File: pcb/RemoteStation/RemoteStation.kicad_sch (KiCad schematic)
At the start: 4 parts, among them J1 Conn_01x04, J2 Conn_01x02, J3 Conn_01x02, J4 Conn_01x04

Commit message: update
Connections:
- no-connect marks 0 -> 14
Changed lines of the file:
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@@
 	(generator_version "8.0")
 	(paper "A4")
+	(no_connect
+		(at 43.18 97.79)
+	)
+	(no_connect
+		(at 158.75 53.34)
+	)
+	(no_connect
+		(at 63.5 97.79)
+	)
+	(no_connect
+		(at 180.34 53.34)
+	)
+	(no_connect
+		(at 58.42 97.79)
+	)
+	(no_connect
+		(at 66.04 97.79)
+	)
+	(no_connect
+		(at 203.2 53.34)
+	)
+	(no_connect
+		(at 156.21 53.34)
+	)
+	(no_connect
+		(at 110.49 53.34)
+	)
+	(no_connect
+		(at 107.95 53.34)
+	)
+	(no_connect
+		(at 60.96 97.79)
+	)
+	(no_connect
+		(at 45.72 97.79)
+	)
+	(no_connect
+		(at 177.8 53.34)
+	)
+	(no_connect
+		(at 205.74 53.34)
+	)
 	(wire
 		(pts
@@
 		(pts
 			(xy 54.61 64.77) (xy 54.61 62.23)
+		)
+		(stroke
+			(width 0)
+			(type default)
+		)
+	)
+	(wire
+		(pts
+			(xy 29.21 173.99) (xy 29.21 176.53)
 		)
 		(stroke
@@
 	)
 	(symbol
+		(lib_id "power:PWR_FLAG")
+		(at 29.21 173.99 0)
+		(unit 1)
+		(exclude_from_sim no)
+		(in_bom yes)
+		(on_board yes)
+		(dnp no)
+		(fields_autoplaced yes)
+		(property "Reference" "#FLG01"
+			(at 29.21 172.085 0)
+			(effects
+				(font
+					(size 1.27 1.27)
+				)
+				(hide yes)
+			)
+		)
+		(property "Value" "PWR_FLAG"
+			(at 29.21 168.91 0)
+			(effects
+				(font
+					(size 1.27 1.27)
+				)
+			)
+		)
+		(property "Footprint" ""
+			(at 29.21 173.99 0)
+			(effects
+				(font
+					(size 1.27 1.27)
+				)
+				(hide yes)
+			)
+		)
+		(property "Datasheet" "~"
+			(at 29.21 173.99 0)
+			(effects
+				(font
+					(size 1.27 1.27)
+				)
+				(hide yes)
+			)
+		)
+		(property "Description" "Special symbol for telling ERC where power comes from"
+			(at 29.21 173.99 0)
+			(effects
+				(font
+					(size 1.27 1.27)
+				)
+				(hide yes)
+			)
+		)
+		(pin "1"
+		)
+		(instances
+			(project "RemoteStation"
+				(path "/5d20b266-567e-45c6-9e3e-145c2aea1daa"
+					(reference "#FLG01")
+					(unit 1)
+				)
+			)
+		)
+	)
+	(symbol
 		(lib_id "Connector_Generic:Conn_01x02")
 		(at 43.18 92.71 90)
@@
 					(unit 1)
 				)
+			)
+		)
+	)
+	(symbol
+		(lib_id "power:GND")
+		(at 29.21 176.53 0)
+		(unit 1)
+		(exclude_from_sim no)
+		(in_bom yes)
+		(on_board yes)
+		(dnp no)
+		(fields_autoplaced yes)
+		(property "Reference" "#PWR018"
+			(at 29.21 182.88 0)
+			(effects
+				(font
+					(size 1.27 1.27)
+				)
+				(hide yes)
+			)
+		)
+		(property "Value" "GND"
+			(at 29.21 181.61 0)
+			(effects
+				(font
+					(size 1.27 1.27)
+				)
+			)
+		)
+		(property "Footprint" ""
+			(at 29.21 176.53 0)
+			(effects
+				(font
+					(size 1.27 1.27)
+				)
+				(hide yes)
+			)
+		)
+		(property "Datasheet" ""
+			(at 29.21 176.53 0)
+			(effects
+				(font
+					(size 1.27 1.27)
+				)
+				(hide yes)
+			)
+		)
+		(property "Description" "Power symbol creates a global label with name \"GND\" , ground"
+			(at 29.21 176.53 0)
+			(effects
+				(font
+					(size 1.27 1.27)
+				)
+				(hide yes)
+			)
+		)
+		(pin "1"
+		)
+		(instances
+			(project "RemoteStation"
+				(path "/5d20b266-567e-45c6-9e3e-145c2aea1daa"
+					(reference "#PWR018")
+					(unit 1)
+				)

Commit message: update scripts
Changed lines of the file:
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@@
-	(wire
-		(pts
-			(xy 29.21 173.99) (xy 29.21 176.53)
-		)
-		(stroke
-			(width 0)
-			(type default)
-		)
-	)
 	(wire
 		(pts
@@
 	)
 	(symbol
-		(lib_id "power:PWR_FLAG")
-		(at 29.21 173.99 0)
-		(unit 1)
-		(exclude_from_sim no)
-		(in_bom yes)
-		(on_board yes)
-		(dnp no)
-		(fields_autoplaced yes)
-		(property "Reference" "#FLG01"
-			(at 29.21 172.085 0)
-			(effects
-				(font
-					(size 1.27 1.27)
-				)
-				(hide yes)
-			)
-		)
-		(property "Value" "PWR_FLAG"
-			(at 29.21 168.91 0)
-			(effects
-				(font
-					(size 1.27 1.27)
-				)
-			)
-		)
-		(property "Footprint" ""
-			(at 29.21 173.99 0)
-			(effects
-				(font
-					(size 1.27 1.27)
-				)
-				(hide yes)
-			)
-		)
-		(property "Datasheet" "~"
-			(at 29.21 173.99 0)
-			(effects
-				(font
-					(size 1.27 1.27)
-				)
-				(hide yes)
-			)
-		)
-		(property "Description" "Special symbol for telling ERC where power comes from"
-			(at 29.21 173.99 0)
-			(effects
-				(font
-					(size 1.27 1.27)
-				)
-				(hide yes)
-			)
-		)
-		(pin "1"
-		)
-		(instances
-			(project "RemoteStation"
-				(path "/5d20b266-567e-45c6-9e3e-145c2aea1daa"
-					(reference "#FLG01")
-					(unit 1)
-				)
-			)
-		)
-	)
-	(symbol
 		(lib_id "Connector_Generic:Conn_01x02")
 		(at 43.18 92.71 90)
@@
 					(unit 1)
 				)
-			)
-		)
-	)
-	(symbol
-		(lib_id "power:GND")
-		(at 29.21 176.53 0)
-		(unit 1)
-		(exclude_from_sim no)
-		(in_bom yes)
-		(on_board yes)
-		(dnp no)
-		(fields_autoplaced yes)
-		(property "Reference" "#PWR018"
-			(at 29.21 182.88 0)
-			(effects
-				(font
-					(size 1.27 1.27)
-				)
-				(hide yes)
-			)
-		)
-		(property "Value" "GND"
-			(at 29.21 181.61 0)
-			(effects
-				(font
-					(size 1.27 1.27)
-				)
-			)
-		)
-		(property "Footprint" ""
-			(at 29.21 176.53 0)
-			(effects
-				(font
-					(size 1.27 1.27)
-				)
-				(hide yes)
-			)
-		)
-		(property "Datasheet" ""
-			(at 29.21 176.53 0)
-			(effects
-				(font
-					(size 1.27 1.27)
-				)
-				(hide yes)
-			)
-		)
-		(property "Description" "Power symbol creates a global label with name \"GND\" , ground"
-			(at 29.21 176.53 0)
-			(effects
-				(font
-					(size 1.27 1.27)
-				)
-				(hide yes)
-			)
-		)
-		(pin "1"
-		)
-		(instances
-			(project "RemoteStation"
-				(path "/5d20b266-567e-45c6-9e3e-145c2aea1daa"
-					(reference "#PWR018")
-					(unit 1)
-				)

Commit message: big update
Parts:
- removed J4: Conn_01x04, Connector_PinHeader_2.54mm:PinHeader_1x04_P2.54mm_Horizontal, symbol Connector_Generic:Conn_01x04
- added J104: Conn_01x05, symbol Connector_Generic:Conn_01x05
- added J105, J107, J109, J111: Conn_01x02, Connector_PinSocket_2.54mm:PinSocket_1x02_P2.54mm_Vertical, symbol Connector_Generic:Conn_01x02
- added J106, J108, J110, J112: Conn_01x04, Connector_PinHeader_2.54mm:PinHeader_1x04_P2.54mm_Vertical, symbol Connector_Generic:Conn_01x04
- renumbered J3 to J101, J2 to J102, J1 to J103
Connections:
- net Bus/+5V: now also J106.4 (Pin_4), J108.4 (Pin_4), J110.4 (Pin_4), J112.4 (Pin_4)
- net Bus/USB1_D+: now also J106.3 (Pin_3)
- net Bus/USB1_D-: now also J106.2 (Pin_2)
- net Bus/USB2_D+: now also J108.3 (Pin_3)
- net Bus/USB2_D-: now also J108.2 (Pin_2)
- net Bus/USB3_D+: now also J110.3 (Pin_3)
- net Bus/USB3_D-: now also J110.2 (Pin_2)
- net Bus/USB4_D+: now also J112.3 (Pin_3)
- net Bus/USB4_D-: now also J112.2 (Pin_2)
- net GND: now also J101.2 (Pin_2), J104.4 (Pin_4), J105.1 (Pin_1), J106.1 (Pin_1), J107.1 (Pin_1), J108.1 (Pin_1), J109.1 (Pin_1), J110.1 (Pin_1), J111.1 (Pin_1), J112.1 (Pin_1)
- net Raspberry Pi/+12V: now reaches J101.1 (Pin_1)
- net Bus/VCC renamed Bus/+12V
- net Bus/+12V: now also J105.2 (Pin_2), J107.2 (Pin_2), J109.2 (Pin_2), J111.2 (Pin_2)
- new net Raspberry Pi/+5V: J104.1 (Pin_1)
- new net Raspberry Pi/USB+: J104.2 (Pin_2)
- new net Raspberry Pi/USB-: J104.3 (Pin_3)
- new net Raspberry Pi/USB_OTG_ID: J104.5 (Pin_5)
- no-connect marks 14 -> 0
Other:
- removed sheet VHF
- sheet Bus ports: added +12V; removed VCC
- sheet Raspberry Pi ports: added +12V, +5V, USB+, USB-, USB_OTG_ID; removed none
- moved on the sheet: J101, J102, J103

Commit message: add hash
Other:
- note added: "<<HASH>>"
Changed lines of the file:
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@@
+		)
+	)
+	(text "<<HASH>>"
+		(exclude_from_sim no)
+		(at 267.97 193.548 0)
+		(effects
+			(font
+				(size 1.27 1.27)
+			)
+			(justify left)
 		)
 	)

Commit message: add hash and title
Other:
- note added: "Amateurfunkclub fuer Remote Stationen"
- note added: "Remote Station"
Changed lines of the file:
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@@
+		)
+	)
+	(text "Remote Station"
+		(exclude_from_sim no)
+		(at 178.816 171.196 0)
+		(effects
+			(font
+				(size 5 5)
+			)
+			(justify left)
+		)
+	)
+	(text "Amateurfunkclub fuer Remote Stationen"
+		(exclude_from_sim no)
+		(at 186.436 189.992 0)
+		(effects
+			(font
+				(size 1.27 1.27)
+			)
+			(justify left)
 		)
 	)

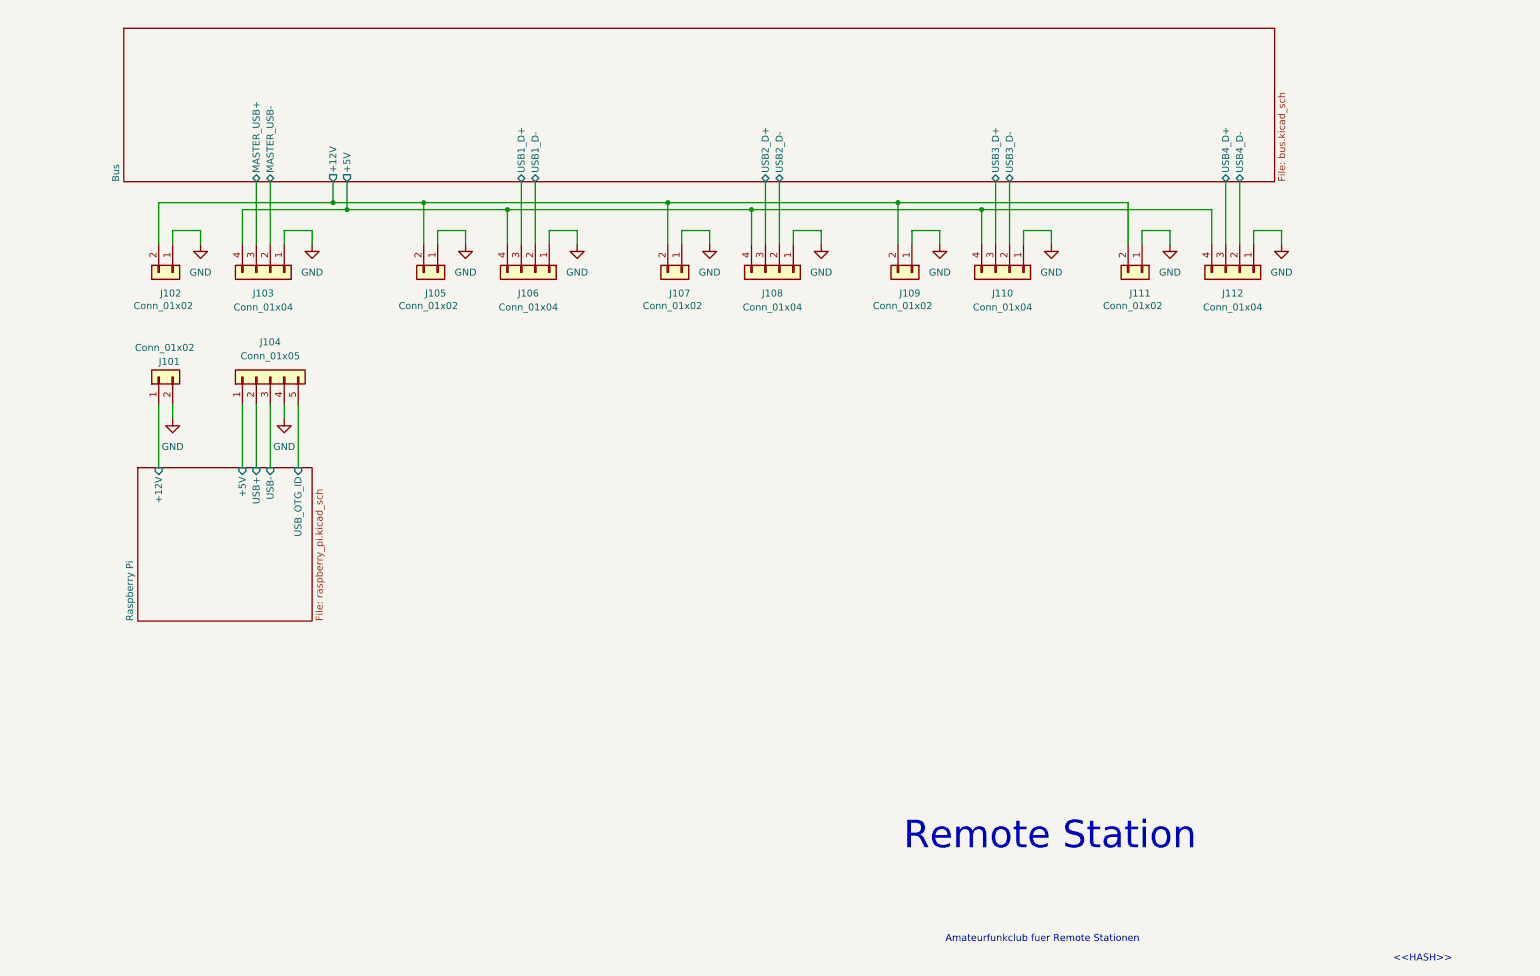
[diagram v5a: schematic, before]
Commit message: update connectors
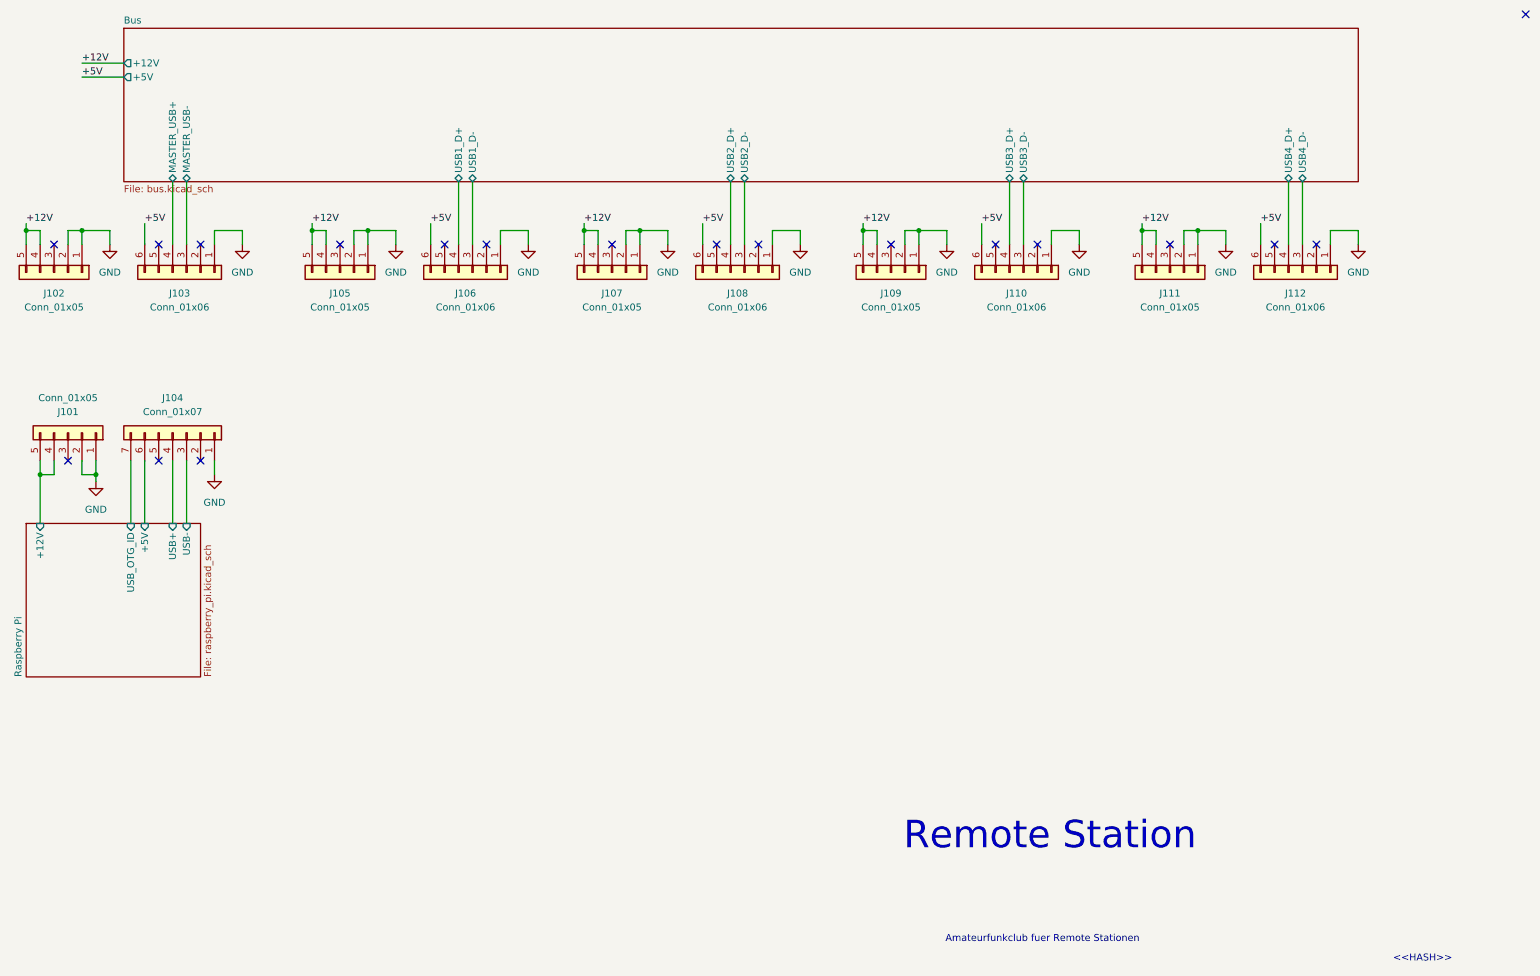
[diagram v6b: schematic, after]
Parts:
- removed J101: Conn_01x02, Connector_PinHeader_2.54mm:PinHeader_1x02_P2.54mm_Horizontal, symbol Connector_Generic:Conn_01x02
- removed J102, J105, J107, J109, J111: Conn_01x02, Connector_PinSocket_2.54mm:PinSocket_1x02_P2.54mm_Vertical, symbol Connector_Generic:Conn_01x02
- removed J103, J106, J108, J110, J112: Conn_01x04, Connector_PinHeader_2.54mm:PinHeader_1x04_P2.54mm_Vertical, symbol Connector_Generic:Conn_01x04
- removed J104: Conn_01x05, symbol Connector_Generic:Conn_01x05
- added J101, J102, J105, J107, J109, J111: Conn_01x05, symbol Connector_Generic:Conn_01x05
- added J103, J106, J108, J110, J112: Conn_01x06, symbol Connector_Generic:Conn_01x06
- added J104: Conn_01x07, symbol Connector_Generic:Conn_01x07
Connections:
- net Bus/MASTER_USB+: now also J103.4 (Pin_4)
- net Bus/MASTER_USB-: now also J103.3 (Pin_3)
- net Bus/USB1_D+: now also J106.4 (Pin_4)
- net Bus/USB1_D-: now also J106.3 (Pin_3)
- net Bus/USB2_D+: now also J108.4 (Pin_4)
- net Bus/USB2_D-: now also J108.3 (Pin_3)
- net Bus/USB3_D+: now also J110.4 (Pin_4)
- net Bus/USB3_D-: now also J110.3 (Pin_3)
- net Bus/USB4_D+: now also J112.4 (Pin_4)
- net Bus/USB4_D-: now also J112.3 (Pin_3)
- net GND: now also J101.1 (Pin_1), J101.2 (Pin_2), J102.1 (Pin_1), J102.2 (Pin_2), J103.1 (Pin_1), J104.1 (Pin_1), J105.1 (Pin_1), J105.2 (Pin_2), J106.1 (Pin_1), J107.1 (Pin_1), J107.2 (Pin_2), J108.1 (Pin_1), J109.1 (Pin_1), J109.2 (Pin_2), J110.1 (Pin_1), J111.1 (Pin_1), J111.2 (Pin_2), J112.1 (Pin_1)
- net Raspberry Pi/+12V: now also J101.4 (Pin_4), J101.5 (Pin_5)
- net Raspberry Pi/+5V: now also J104.6 (Pin_6)
- net Raspberry Pi/USB+: now also J104.4 (Pin_4)
- net Raspberry Pi/USB-: now also J104.3 (Pin_3)
- net Raspberry Pi/USB_OTG_ID: now also J104.7 (Pin_7)
- new net +12V: J102.4 (Pin_4), J102.5 (Pin_5), J105.4 (Pin_4), J105.5 (Pin_5), J107.4 (Pin_4), J107.5 (Pin_5), J109.4 (Pin_4), J109.5 (Pin_5), J111.4 (Pin_4), J111.5 (Pin_5)
- new net +5V: J103.6 (Pin_6), J106.6 (Pin_6), J108.6 (Pin_6), J110.6 (Pin_6), J112.6 (Pin_6)
- no-connect marks 0 -> 19
